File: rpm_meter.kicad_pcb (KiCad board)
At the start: 2 copper layers, 122.3 x 96.7 mm, 246 parts, among them IC1 STPIC6D595TTR, IC2 STPIC6D595TTR, IC3 STPIC6D595TTR, IC4 STPIC6D595TTR, IC5 STPIC6D595TTR, IC6 TPS566247DRLR, J1 Conn_01x05_Pin, Q1 BC846, Q10 BC857, Q12 BC846, Q13 AO3423, Q14 BC846, Q15 BC846, Q16 BC846, Q17 BC857, Q19 BC857, Q2 BC857, Q21 BC857, Q23 BC857, Q25 BC857, Q27 BC857, Q29 BC857, Q31 BC857, Q33 BC857, Q35 BC857, Q37 BC857, Q39 BC857, Q4 BC857, Q41 BC857, Q43 BC857, Q45 BC857, Q47 BC857, Q49 BC857, Q51 BC857, Q53 BC857, Q55 BC857, Q57 BC857, Q59 BC857, Q6 BC857, Q61 BC857, Q63 BC857, Q65 BC857, Q67 BC857, Q69 BC857, Q71 BC857, Q73 BC857, Q75 BC857, Q77 BC857, Q79 BC857, Q8 BC857, Q81 BC857, Q83 BC857, Q85 BC857, U1 M24C02-RMN, U2 STM32C031C6Tx, U3 74LVC1G123, U4 TLV1117-33, Y1 8

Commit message: ws2812b
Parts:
- removed C17, C18, C19, C20, C21: 100n, Capacitor_SMD:C_0603_1608Metric
- removed IC2, IC3, IC4, IC5: STPIC6D595TTR, Library_local:SOP65P640X120-16N
- removed Q10, Q17, Q19, Q2, Q21, Q23, Q25, Q27, Q29, Q31, Q33, Q35, Q37, Q39, Q4, Q41, Q43, Q45, Q47, Q49, Q51, Q53, Q55, Q57, Q59, Q6, Q61, Q63, Q65, Q67, Q69, Q71, Q73, Q75, Q77, Q79, Q8, Q81, Q83, Q85: BC857, Package_TO_SOT_SMD:SOT-23
- removed R10, R101, R107, R113, R119, R125, R131, R137, R143, R149, R155, R16, R22, R28, R34, R40, R46, R83, R89, R95: 91, Resistor_SMD:R_0603_1608Metric
- removed R102, R108, R11, R114, R120, R126, R132, R138, R144, R150, R156, R17, R23, R29, R35, R41, R78, R84, R90, R96: 22, Resistor_SMD:R_0603_1608Metric
- removed R103, R109, R115, R12, R121, R127, R133, R139, R145, R151, R157, R18, R24, R30, R36, R42, R79, R85, R91, R97: 100, Resistor_SMD:R_0603_1608Metric
- removed R104, R110, R116, R122, R128, R13, R134, R140, R146, R152, R19, R25, R31, R37, R43, R7, R8, R80, R86, R92, R98: 10k, Resistor_SMD:R_0603_1608Metric
- D10, D11, D12, D13, D14, D15, D16, D17, D18, D19, D20, D21, D22, D3, D4, D5, D6, D7, D8, D9: value LED_Dual_AAKK -> WS2812B; footprint Library_local:LED_RG_1210 -> LED_SMD:LED_WS2812B_PLCC4_5.0x5.0mm_P3.2mm
- IC1: value STPIC6D595TTR -> SN74LV1T34DCKR; footprint Library_local:SOP65P640X120-16N -> Library_local:SOT65P210X110-5N
- U3: footprint Package_SO:MSOP-8-1EP_3x3mm_P0.65mm_EP1.5x1.8mm -> Package_SO:SSOP-8_2.95x2.8mm_P0.65mm
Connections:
- net /Leds/MOSI renamed /Leds/WS2812B_IN
- D10 pad 1: /Leds/led_segment7/led_net_2_1 -> +5V
- D10 pad 2: /Leds/led_segment7/led_net_2_1 -> Net-(D10-DOUT)
- D10 pad 3: /Leds/led_segment7/led_net_2_2 -> GND
- D10 pad 4: /Leds/led_segment7/led_net_2_4 -> Net-(D10-DIN)
- D11 pad 1: /Leds/led_segment8/led_net_2_1 -> +5V
- D11 pad 2: /Leds/led_segment8/led_net_2_1 -> Net-(D11-DOUT)
- D11 pad 3: /Leds/led_segment8/led_net_2_2 -> GND
- D11 pad 4: /Leds/led_segment8/led_net_2_4 -> Net-(D10-DOUT)
- D12 pad 1: /Leds/led_segment9/led_net_2_1 -> +5V
- D12 pad 2: /Leds/led_segment9/led_net_2_1 -> Net-(D12-DOUT)
- D12 pad 3: /Leds/led_segment9/led_net_2_2 -> GND
- D12 pad 4: /Leds/led_segment9/led_net_2_4 -> Net-(D11-DOUT)
- D13 pad 1: /Leds/led_segment10/led_net_2_1 -> +5V
- D13 pad 2: /Leds/led_segment10/led_net_2_1 -> Net-(D13-DOUT)
- D13 pad 3: /Leds/led_segment10/led_net_2_2 -> GND
- D13 pad 4: /Leds/led_segment10/led_net_2_4 -> Net-(D12-DOUT)
- D14 pad 1: /Leds/led_segment11/led_net_2_1 -> +5V
- D14 pad 2: /Leds/led_segment11/led_net_2_1 -> Net-(D14-DOUT)
- D14 pad 3: /Leds/led_segment11/led_net_2_2 -> GND
- D14 pad 4: /Leds/led_segment11/led_net_2_4 -> Net-(D13-DOUT)
- D15 pad 1: /Leds/led_segment12/led_net_2_1 -> +5V
- D15 pad 2: /Leds/led_segment12/led_net_2_1 -> Net-(D15-DOUT)
- D15 pad 3: /Leds/led_segment12/led_net_2_2 -> GND
- D15 pad 4: /Leds/led_segment12/led_net_2_4 -> Net-(D14-DOUT)
- D16 pad 1: /Leds/led_segment13/led_net_2_1 -> +5V
- D16 pad 2: /Leds/led_segment13/led_net_2_1 -> Net-(D16-DOUT)
- D16 pad 3: /Leds/led_segment13/led_net_2_2 -> GND
- D16 pad 4: /Leds/led_segment13/led_net_2_4 -> Net-(D15-DOUT)
- D17 pad 1: /Leds/led_segment14/led_net_2_1 -> +5V
- D17 pad 2: /Leds/led_segment14/led_net_2_1 -> Net-(D17-DOUT)
- D17 pad 3: /Leds/led_segment14/led_net_2_2 -> GND
- D17 pad 4: /Leds/led_segment14/led_net_2_4 -> Net-(D16-DOUT)
- D18 pad 1: /Leds/led_segment15/led_net_2_1 -> +5V
- D18 pad 2: /Leds/led_segment15/led_net_2_1 -> Net-(D18-DOUT)
- D18 pad 3: /Leds/led_segment15/led_net_2_2 -> GND
- D18 pad 4: /Leds/led_segment15/led_net_2_4 -> Net-(D17-DOUT)
- D19 pad 1: /Leds/led_segment16/led_net_2_1 -> +5V
- D19 pad 2: /Leds/led_segment16/led_net_2_1 -> Net-(D19-DOUT)
- D19 pad 3: /Leds/led_segment16/led_net_2_2 -> GND
- D19 pad 4: /Leds/led_segment16/led_net_2_4 -> Net-(D18-DOUT)
- D20 pad 1: /Leds/led_segment17/led_net_2_1 -> +5V
- D20 pad 2: /Leds/led_segment17/led_net_2_1 -> Net-(D20-DOUT)
- D20 pad 3: /Leds/led_segment17/led_net_2_2 -> GND
- D20 pad 4: /Leds/led_segment17/led_net_2_4 -> Net-(D19-DOUT)
- D21 pad 1: /Leds/led_segment18/led_net_2_1 -> +5V
- D21 pad 2: /Leds/led_segment18/led_net_2_1 -> Net-(D21-DOUT)
- D21 pad 3: /Leds/led_segment18/led_net_2_2 -> GND
- D21 pad 4: /Leds/led_segment18/led_net_2_4 -> Net-(D20-DOUT)
- D22 pad 1: /Leds/led_segment19/led_net_2_1 -> +5V
- D22 pad 2: /Leds/led_segment19/led_net_2_1 -> unconnected-(D22-DOUT-Pad2)
- D22 pad 3: /Leds/led_segment19/led_net_2_2 -> GND
- D22 pad 4: /Leds/led_segment19/led_net_2_4 -> Net-(D21-DOUT)
- D3 pad 1: /Leds/led_segment0/led_net_2_1 -> +5V
- D3 pad 2: /Leds/led_segment0/led_net_2_1 -> Net-(D3-DOUT)
- D3 pad 3: /Leds/led_segment0/led_net_2_2 -> GND
- D3 pad 4: /Leds/led_segment0/led_net_2_4 -> Net-(D3-DIN)
- D4 pad 1: /Leds/led_segment1/led_net_2_1 -> +5V
- D4 pad 2: /Leds/led_segment1/led_net_2_1 -> Net-(D4-DOUT)
- D4 pad 3: /Leds/led_segment1/led_net_2_2 -> GND
- D4 pad 4: /Leds/led_segment1/led_net_2_4 -> Net-(D3-DOUT)
- D5 pad 1: /Leds/led_segment2/led_net_2_1 -> +5V
- D5 pad 2: /Leds/led_segment2/led_net_2_1 -> Net-(D5-DOUT)
- D5 pad 3: /Leds/led_segment2/led_net_2_2 -> GND
- D5 pad 4: /Leds/led_segment2/led_net_2_4 -> Net-(D4-DOUT)
- D6 pad 1: /Leds/led_segment3/led_net_2_1 -> +5V
- D6 pad 2: /Leds/led_segment3/led_net_2_1 -> Net-(D6-DOUT)
- D6 pad 3: /Leds/led_segment3/led_net_2_2 -> GND
- D6 pad 4: /Leds/led_segment3/led_net_2_4 -> Net-(D5-DOUT)
- D7 pad 1: /Leds/led_segment4/led_net_2_1 -> +5V
- D7 pad 2: /Leds/led_segment4/led_net_2_1 -> Net-(D7-DOUT)
- D7 pad 3: /Leds/led_segment4/led_net_2_2 -> GND
- D7 pad 4: /Leds/led_segment4/led_net_2_4 -> Net-(D6-DOUT)
- D8 pad 1: /Leds/led_segment5/led_net_2_1 -> +5V
- D8 pad 2: /Leds/led_segment5/led_net_2_1 -> Net-(D8-DOUT)
- D8 pad 3: /Leds/led_segment5/led_net_2_2 -> GND
- D8 pad 4: /Leds/led_segment5/led_net_2_4 -> Net-(D7-DOUT)
- D9 pad 1: /Leds/led_segment6/led_net_2_1 -> +5V
- D9 pad 2: /Leds/led_segment6/led_net_2_1 -> Net-(D10-DIN)
- D9 pad 3: /Leds/led_segment6/led_net_2_2 -> GND
- D9 pad 4: /Leds/led_segment6/led_net_2_4 -> Net-(D8-DOUT)
- IC1 pad 1: +5V -> unconnected-(IC1-N.C-Pad1)
- IC1 pad 3: /Leds/green0 -> GND
- IC1 pad 4: /Leds/red0 -> Net-(D3-DIN)
- IC1 pad 5: /Leds/green1 -> +5V
- U2 pad 11: /mcu/enc_a -> /alert_yellow/sig_to_mcu
- U2 pad 12: /mcu/enc_b -> /alert_red/sig_to_mcu
- U2 pad 13: /mcu/enc_p -> /light/sig_to_mcu
- U2 pad 14: /light/sig_to_mcu -> unconnected-(U2-PA3-Pad14)
- U2 pad 15: /led_pwm_5v/led_pwm_signal -> /mcu/rpm_signal_mcu
- U2 pad 16: /alert_yellow/sig_to_mcu -> unconnected-(U2-PA5-Pad16)
- U2 pad 17: /mcu/rpm_signal_mcu -> /mcu/enc_a
- U2 pad 18: /alert_red/sig_to_mcu -> /mcu/enc_b
- U2 pad 39: unconnected-(U2-PD1-Pad39) -> /led_pwm_5v/led_pwm_signal
- U2 pad 41: unconnected-(U2-PD3-Pad41) -> /mcu/enc_p
- U2 pad 44: unconnected-(U2-PB5-Pad44) -> /mcu/SPI_MOSI
- U2 pad 45: unconnected-(U2-PB6-Pad45) -> /mcu/SPI_SCK
- U2 pad 46: unconnected-(U2-PB7-Pad46) -> /mcu/LATCH_PIN

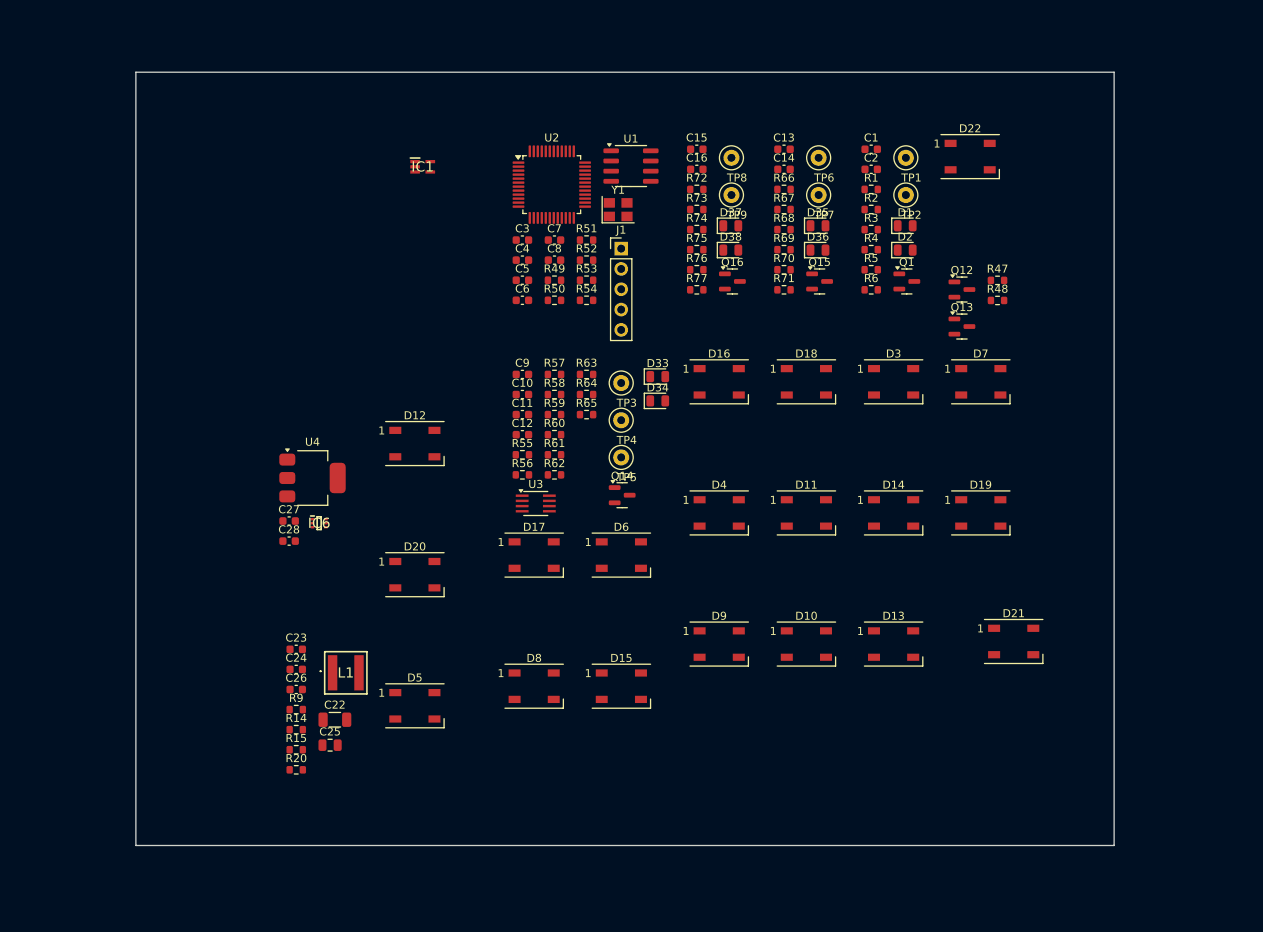
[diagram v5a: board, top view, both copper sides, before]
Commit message: TVS protection
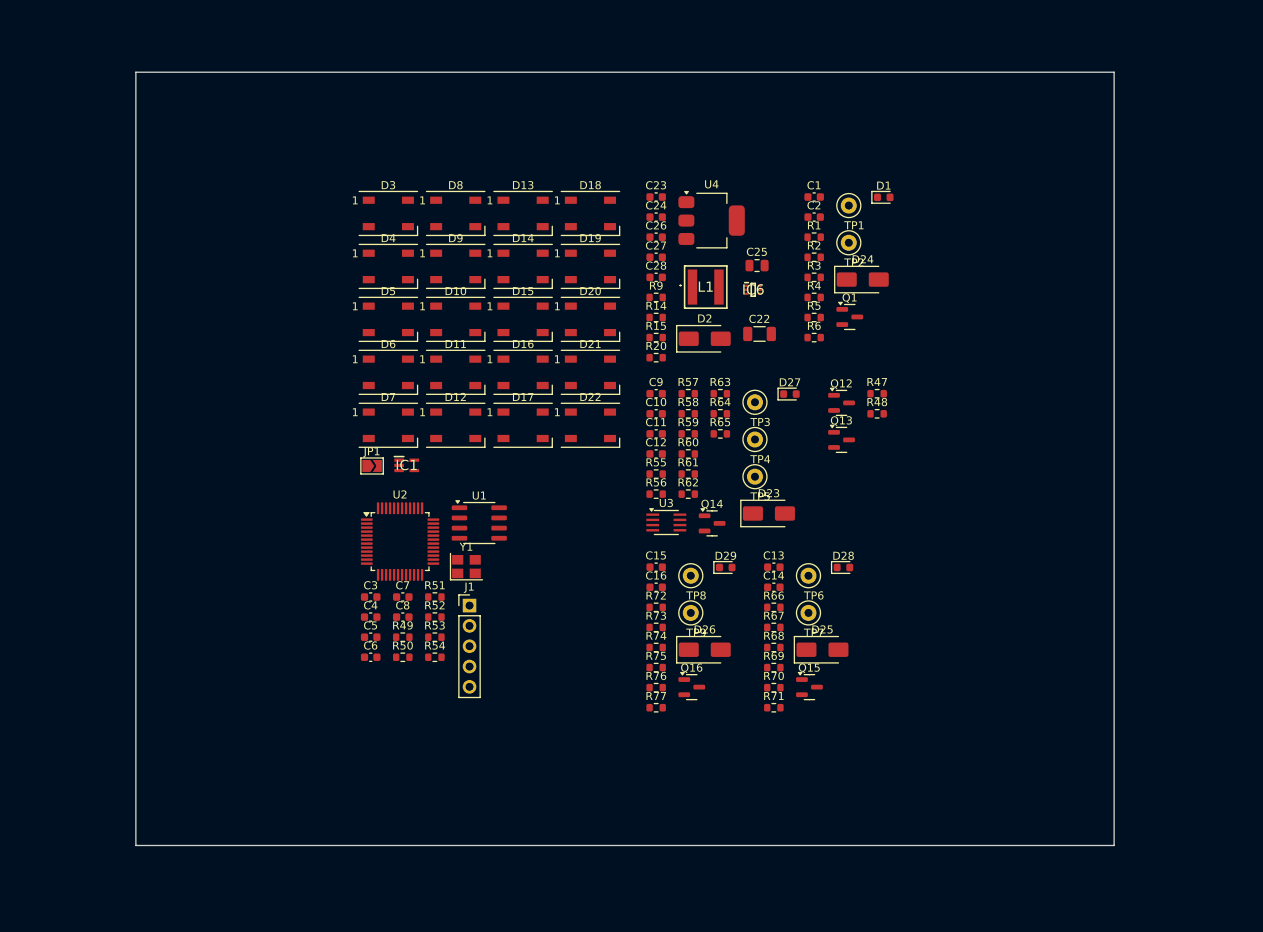
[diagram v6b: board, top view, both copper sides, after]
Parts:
- removed D33, D35, D37: D, Diode_SMD:D_0805_2012Metric
- removed D34, D36, D38: 5.1, Diode_SMD:D_0805_2012Metric
- added D23: SMAJ5.0CA, Diode_SMD:D_SMA, F.Cu at (162.2, 91.8)
- added D24: SMAJ5.0CA, Diode_SMD:D_SMA, F.Cu at (173.9, 62.6)
- added D25: SMAJ5.0CA, Diode_SMD:D_SMA, F.Cu at (168.9, 108.8)
- added D26: SMAJ5.0CA, Diode_SMD:D_SMA, F.Cu at (154.2, 108.8)
- added D27: D_Schottky, Diode_SMD:D_0603_1608Metric, F.Cu at (164.8, 76.9)
- added D28: D_Schottky, Diode_SMD:D_0603_1608Metric, F.Cu at (171.5, 98.6)
- added D29: D_Schottky, Diode_SMD:D_0603_1608Metric, F.Cu at (156.8, 98.6)
- added JP1: Jumper_2_Open, Jumper:SolderJumper-2_P1.3mm_Open_TrianglePad1.0x1.5mm, F.Cu at (112.6, 85.9)
- C9: value 10n -> 1n
- D1: value D -> D_Schottky; footprint Diode_SMD:D_0805_2012Metric -> Diode_SMD:D_0603_1608Metric
- D2: value 5.1 -> SMAJ17CA; footprint Diode_SMD:D_0805_2012Metric -> Diode_SMD:D_SMA
- moved C25 80.3 mm to (160.7, 60.8)
- moved D7 74.3 mm to (114.7, 80.8)
- moved C23 72.3 mm to (148.1, 52.2)
- moved C24 72.3 mm to (148.1, 54.8)
- moved C26 72.3 mm to (148.1, 57.3)
- moved C22 71.7 mm to (161.0, 69.4)
- moved D13 71.0 mm to (131.5, 54.3)
- moved R15 68.4 mm to (148.1, 69.8)
- moved R14 68.4 mm to (148.1, 67.3)
- moved R20 68.4 mm to (148.1, 72.3)
- moved R9 68.4 mm to (148.1, 64.8)
- moved D3 66.6 mm to (114.7, 54.3)
- moved L1 65.9 mm to (154.3, 63.5)
- moved D21 62.7 mm to (139.9, 74.2)
- moved IC6 61.6 mm to (160.3, 63.9)
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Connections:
- D2 pad 1: Net-(D1-K) -> GND
- D2 pad 2: GND -> +12V

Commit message: Placed footprints v1.0
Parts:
- removed D1, D28, D29: D_Schottky, Diode_SMD:D_0603_1608Metric
- removed Q12: BC846, Package_TO_SOT_SMD:SOT-23
- removed Q13: AO3423, Package_TO_SOT_SMD:SOT-23
- removed R47: 1k, Resistor_SMD:R_0603_1608Metric
- removed R48, R49, R50, R51: 10k, Resistor_SMD:R_0603_1608Metric
- removed TP1, TP2, TP6, TP7, TP8, TP9: TestPoint, TestPoint:TestPoint_Loop_D1.80mm_Drill1.0mm_Beaded
- added C17: 100n, Capacitor_SMD:C_0603_1608Metric, F.Cu at (209.2, 70.2)
- added J2: Conn_2Rows-05Pins, Connector_PinHeader_2.54mm:PinHeader_2x03_P2.54mm_Vertical, F.Cu at (199.3, 69.1)
- added J3: Conn_01x01_Socket, Connector_Wire:SolderWire-0.15sqmm_1x01_D0.5mm_OD1.5mm, F.Cu at (215.5, 121.8)
- added J4: Conn_01x01_Socket, Connector_Wire:SolderWire-0.15sqmm_1x01_D0.5mm_OD1.5mm, F.Cu at (209.0, 123.3)
- added J5: Conn_01x01_Socket, Connector_Wire:SolderWire-0.15sqmm_1x01_D0.5mm_OD1.5mm, F.Cu at (212.1, 123.3)
- added J6: Conn_01x01_Socket, Connector_Wire:SolderWire-0.15sqmm_1x01_D0.5mm_OD1.5mm, F.Cu at (209.0, 120.5)
- added J7: Conn_01x01_Socket, Connector_Wire:SolderWire-0.15sqmm_1x01_D0.5mm_OD1.5mm, F.Cu at (206.4, 116.7)
- added L2: 6,8u, Inductor_SMD:L_6.3x6.3_H3, F.Cu at (216.7, 113.1)
- added R7: 0,1, Resistor_SMD:R_MELF_MMB-0207, F.Cu at (217.6, 118.6)
- added U5: PEC11R-4225F-S0024, Library_local:PEC12R-4XXXF-SXXXX_1, F.Cu at (205.2, 83.9)
- C10, C3, D25, Q14, R52, R53, R54, R60, R61, R62, R67, U1: moved to B.Cu
- J1: value Conn_01x05_Pin -> Conn_01x01_Socket; footprint Connector_PinHeader_2.54mm:PinHeader_1x05_P2.54mm_Vertical -> Connector_Wire:SolderWire-0.15sqmm_1x01_D0.5mm_OD1.5mm
- R1, R66: footprint Resistor_SMD:R_0603_1608Metric -> Resistor_SMD:R_2512_6332Metric; moved to B.Cu
- R72: footprint Resistor_SMD:R_0603_1608Metric -> Resistor_SMD:R_2512_6332Metric
- moved C3 104.4 mm to (197.0, 41.1)
- moved R54 101.7 mm to (197.0, 42.8), turned to 180 degrees
- moved C6 100.1 mm to (197.6, 57.2), turned to 90 degrees
- moved C5 99.5 mm to (193.4, 49.4), turned to -90 degrees
- moved C4 99.4 mm to (195.0, 49.4), turned to 90 degrees
- moved JP1 99.3 mm to (200.7, 40.0), turned to 165 degrees
- moved R53 99.1 mm to (197.1, 44.4), turned to 180 degrees
- moved C8 98.7 mm to (198.1, 49.4), turned to 90 degrees
- moved IC1 98.6 mm to (207.9, 47.7), turned to 90 degrees
- moved U2 97.1 mm to (204.6, 55.1)
- moved R52 96.6 mm to (197.1, 46.0), turned to 180 degrees
- moved C7 96.0 mm to (196.6, 49.4), turned to 90 degrees
- moved J1 95.7 mm to (218.7, 121.9)
- moved U1 91.6 mm to (203.5, 44.1), turned to 180 degrees
- moved C23 89.8 mm to (209.6, 117.7), turned to 180 degrees
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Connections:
- C1 pad 1: Net-(D1-K) -> Net-(D24-A2)
- C13 pad 1: Net-(D28-K) -> Net-(D25-A2)
- C15 pad 1: Net-(D29-K) -> Net-(D26-A2)
- C22 pad 1: +12V -> Net-(D2-A2)
- C23 pad 1: +12V -> Net-(D2-A2)
- D2 pad 2: +12V -> Net-(D2-A2)
- D24 pad 2: Net-(D1-A) -> Net-(D24-A2)
- IC6 pad 1: +12V -> Net-(IC6-VIN)
- J1 pad 1: /mcu/TMS -> +12V
- R1 pad 2: Net-(D1-A) -> Net-(D24-A2)
- R2 pad 2: Net-(D1-K) -> Net-(D24-A2)
- R3 pad 1: Net-(D1-K) -> Net-(D24-A2)
- R67 pad 2: Net-(D28-K) -> Net-(D25-A2)
- R68 pad 1: Net-(D28-K) -> Net-(D25-A2)
- R73 pad 2: Net-(D29-K) -> Net-(D26-A2)
- R74 pad 1: Net-(D29-K) -> Net-(D26-A2)
- R9 pad 1: +12V -> Net-(IC6-VIN)
- U1 pad 1: Net-(U1-E0) -> GND
- U1 pad 2: Net-(U1-E1) -> GND
- U1 pad 3: Net-(U1-E2) -> GND
- U2 pad 39: /led_pwm_5v/led_pwm_signal -> /mcu/led_pwm_out_3v3
- U3 pad 4: unconnected-(U3B-GND-Pad4) -> GND
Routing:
- net Net-(D4-DOUT): track 0.00 -> 4.45 mm
- net Net-(D10-DOUT): track 0.00 -> 4.21 mm
- net Net-(D8-DOUT): track 0.00 -> 4.19 mm
- net Net-(D10-DIN): track 0.00 -> 4.16 mm
- net Net-(D7-DOUT): track 0.00 -> 4.15 mm
- net Net-(D3-DOUT): track 0.00 -> 4.13 mm
- net Net-(D11-DOUT): track 0.00 -> 4.13 mm
- net Net-(D6-DOUT): track 0.00 -> 4.12 mm
- net Net-(D5-DOUT): track 0.00 -> 4.11 mm
- net Net-(D12-DOUT): track 0.00 -> 4.09 mm
- net Net-(D14-DOUT): track 0.00 -> 4.00 mm
- net Net-(D17-DOUT): track 0.00 -> 3.98 mm
- net Net-(D18-DOUT): track 0.00 -> 3.96 mm
- net Net-(D19-DOUT): track 0.00 -> 3.95 mm
- net Net-(D16-DOUT): track 0.00 -> 3.95 mm
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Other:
- board size 122.3 x 96.7 mm -> 153.8 x 95.2 mm

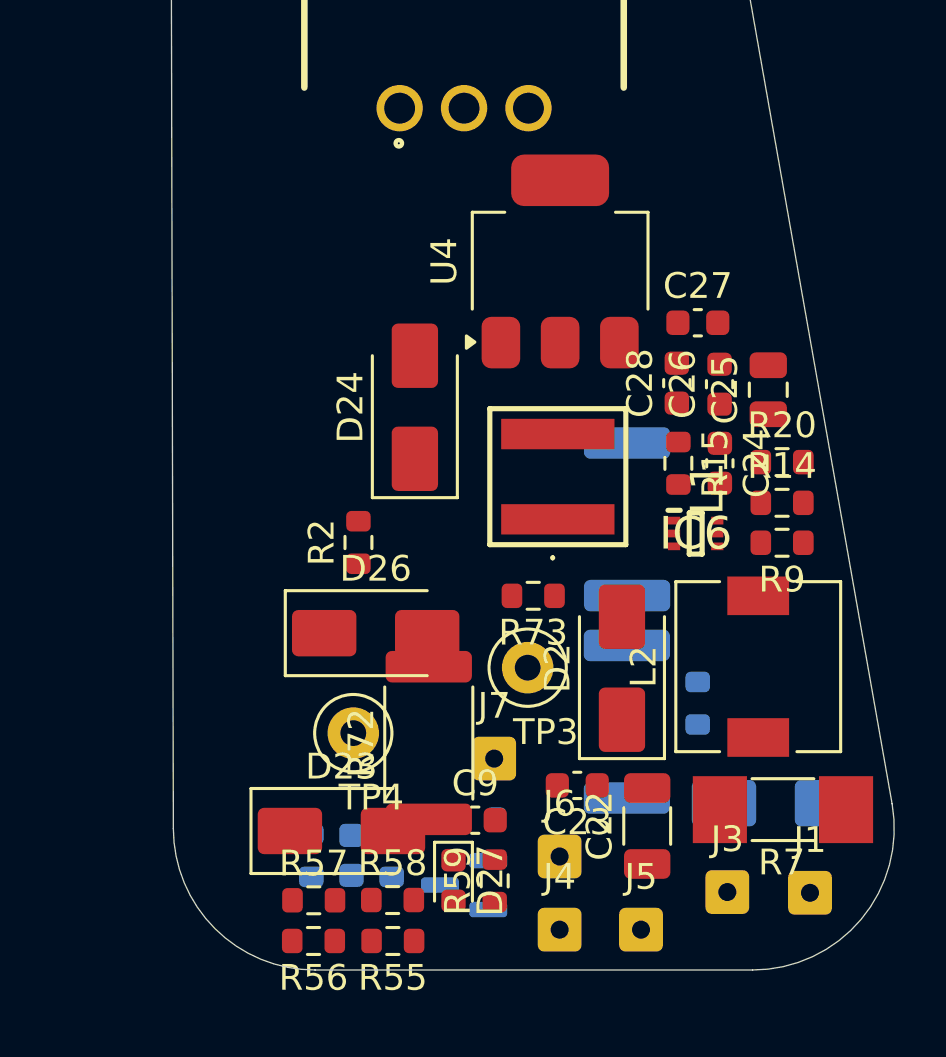
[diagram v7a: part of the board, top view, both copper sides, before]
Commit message: New coils footprint
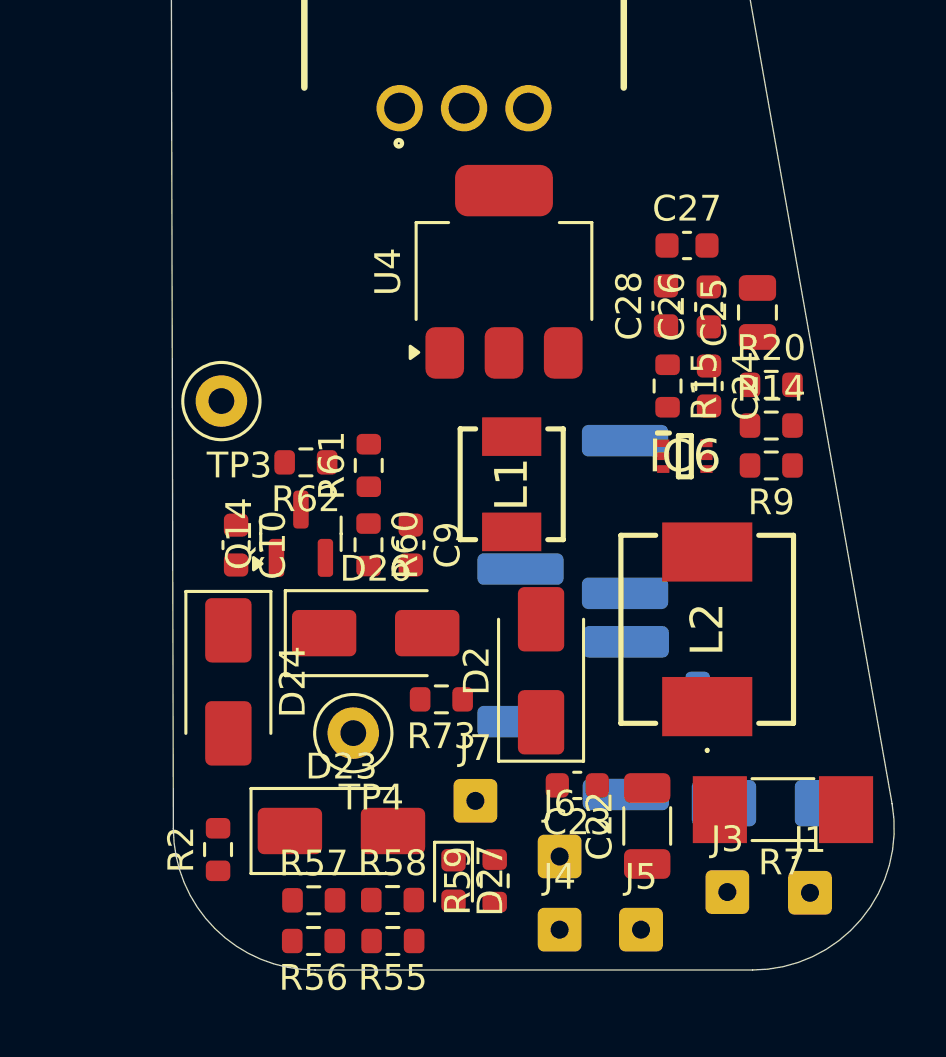
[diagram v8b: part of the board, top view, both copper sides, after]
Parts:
- C10, Q14, R60, R61, R62: moved to F.Cu
- L1: footprint Library_local:XAL5030222MEC -> Library_local:HPI04202R2
- L2: footprint Inductor_SMD:L_6.3x6.3_H3 -> Library_local:HPI06306R8
- R72: moved to B.Cu
- moved TP3 15.8 mm to (195.8, 102.8)
- moved R62 15.3 mm to (199.1, 105.2), turned to 180 degrees
- moved R61 15.2 mm to (201.6, 105.3)
- moved Q14 15.0 mm to (198.9, 107.9), turned to 90 degrees
- moved R2 13.1 mm to (195.7, 120.2)
- moved D24 12.9 mm to (196.1, 113.7), turned to -90 degrees
- moved C10 12.9 mm to (196.4, 108.4), turned to -90 degrees
- moved R60 11.4 mm to (201.5, 108.3), turned to -90 degrees
- moved C9 11.0 mm to (203.2, 108.4), turned to -90 degrees
- moved R73 5.37 mm to (204.4, 114.3)
- moved R72 5.20 mm to (207.4, 112.3)
- moved D2 3.14 mm to (208.2, 113.2)
- moved C24 3.03 mm to (214.8, 102.2)
- moved C25 3.03 mm to (216.6, 99.3)
- moved C26 3.03 mm to (214.8, 99.1)
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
